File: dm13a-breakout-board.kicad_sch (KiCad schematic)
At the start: 6 parts, among them J1 Conn_01x16, J2 Conn_01x02, J3 Conn_01x05

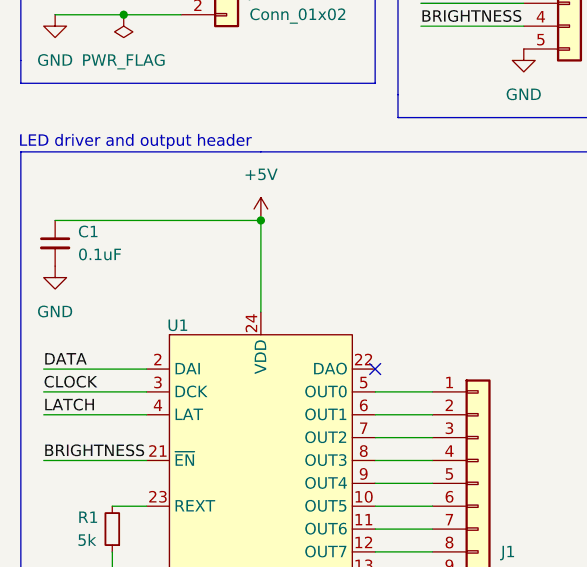
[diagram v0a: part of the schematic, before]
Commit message: Configure BOM stuff
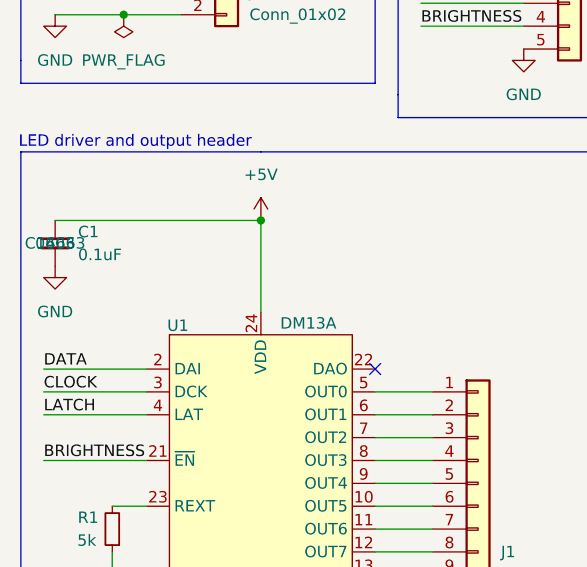
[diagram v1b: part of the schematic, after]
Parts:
- C1: JLCPCB package 0603 -> (none); JLCPCB part number C14663 -> (none); LCSC Part # (none) -> C14663; LCSC package (none) -> 0603
- U1: value ~ -> DM13A
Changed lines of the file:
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@@
-			)
-		)
-		(property "JLCPCB part number" ""
-			(at 24.13 83.82 0)
-			(effects
-				(font
-					(size 1.27 1.27)
-				)
 			)
 		)
@@
 			)
 		)
-		(property "JLCPCB part number" "C14663"
+		(property "LCSC package" "0603"
 			(at 17.78 52.07 0)
 			(effects
@@
 					(size 1.27 1.27)
 				)
-				(hide yes)
-			)
-		)
-		(property "JLCPCB package" "0603"
+			)
+		)
+		(property "LCSC Part #" "C14663"
 			(at 17.78 52.07 0)
 			(effects
@@
 					(size 1.27 1.27)
 				)
-				(hide yes)
 			)
 		)
@@
 			)
 		)
-		(property "JLCPCB part number" ""
-			(at 74.93 25.4 0)
-			(effects
-				(font
-					(size 1.27 1.27)
-				)
-			)
-		)
 		(pin "1"
 		)
@@
 			)
 		)
-		(property "JLCPCB part number" ""
-			(at 36.83 24.13 0)
-			(effects
-				(font
-					(size 1.27 1.27)
-				)
-			)
-		)
 		(pin "1"
 		)
@@
 			)
 		)
-		(property "JLCPCB part number" ""
-			(at 64.77 86.36 0)
-			(effects
-				(font
-					(size 1.27 1.27)
-				)
-			)
-		)
 		(pin "15"
 		)
@@
 			)
 		)
-		(property "Value" "~"
+		(property "Value" "DM13A"
 			(at 42.7833 60.96 0)
 			(effects
@@
 			)
 		)
-		(property "JLCPCB part number" ""
-			(at 40.64 86.36 0)
-			(effects
-				(font
-					(size 1.27 1.27)
-				)
-			)
-		)

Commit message: Try the whole thing
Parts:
- removed J1: Conn_01x16, symbol Connector_Generic:Conn_01x16
- added H1, H2, H3, H4: MountingHole, MountingHole:MountingHole_3.2mm_M3, symbol Mechanical:MountingHole
- added J3, J4: Conn_01x08, Connector_PinHeader_2.54mm:PinHeader_1x08_P2.54mm_Vertical, symbol Connector_Generic:Conn_01x08
- J1: renamed from J2; footprint (none) -> Connector_PinHeader_2.54mm:PinHeader_1x02_P2.54mm_Vertical
- J2: renamed from J3; footprint (none) -> Connector_PinHeader_2.54mm:PinHeader_1x05_P2.54mm_Vertical
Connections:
- net at U1.5 (OUT0): now also J3.1 (Pin_1)
- net at U1.14 (OUT9): now also J4.7 (Pin_7)
- net at U1.15 (OUT10): now also J4.6 (Pin_6)
- net at U1.16 (OUT11): now also J4.5 (Pin_5)
- net at U1.17 (OUT12): now also J4.4 (Pin_4)
- net at U1.18 (OUT13): now also J4.3 (Pin_3)
- net at U1.19 (OUT14): now also J4.2 (Pin_2)
- net at U1.20 (OUT15): now also J4.1 (Pin_1)
- net at U1.6 (OUT1): now also J3.2 (Pin_2)
- net at U1.7 (OUT2): now also J3.3 (Pin_3)
- net at U1.8 (OUT3): now also J3.4 (Pin_4)
- net at U1.9 (OUT4): now also J3.5 (Pin_5)
- net at U1.10 (OUT5): now also J3.6 (Pin_6)
- net at U1.11 (OUT6): now also J3.7 (Pin_7)
- net at U1.12 (OUT7): now also J3.8 (Pin_8)
- net at U1.13 (OUT8): now also J4.8 (Pin_8)
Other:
- note added: "Mounting holes"

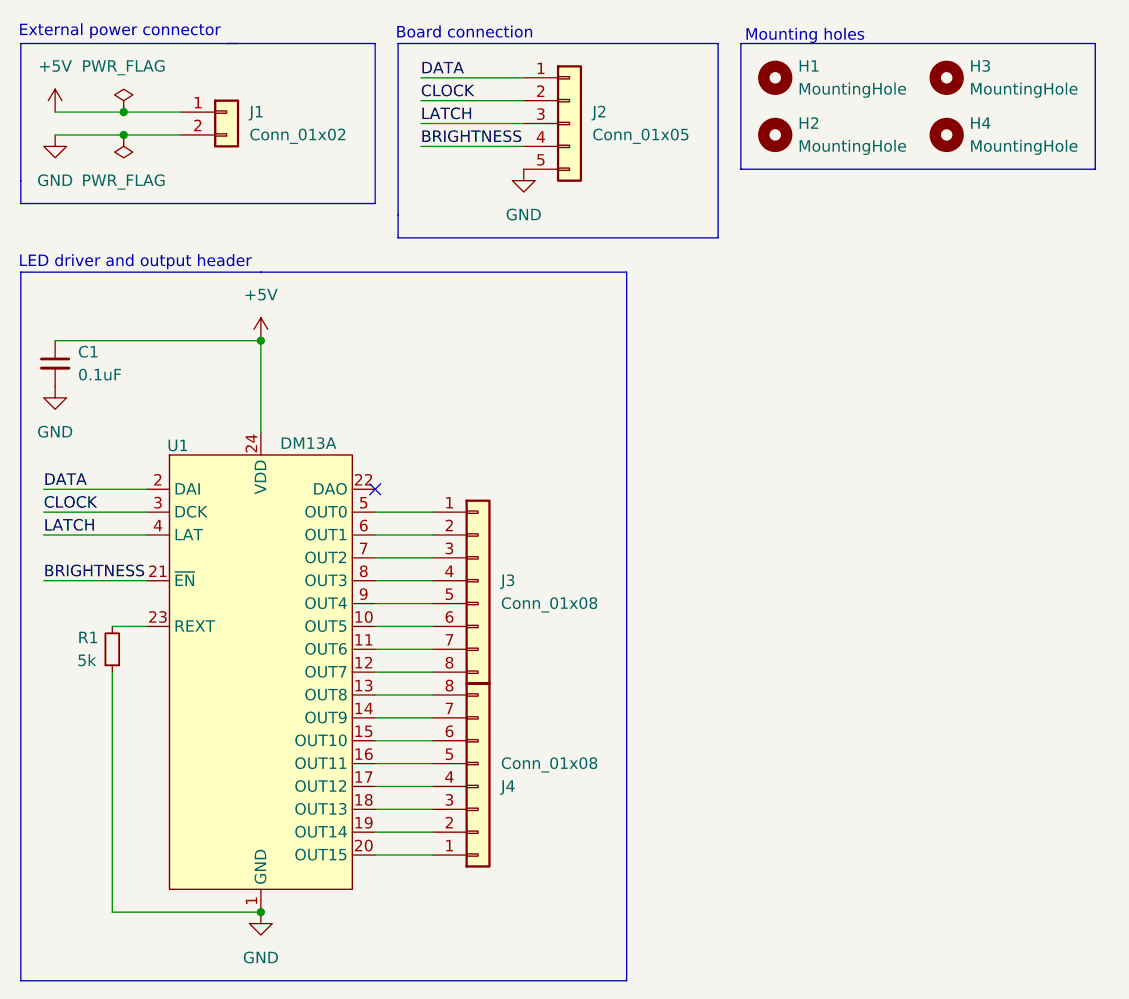
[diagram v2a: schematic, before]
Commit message: Use different connector, add gnd pins, add silkscreen
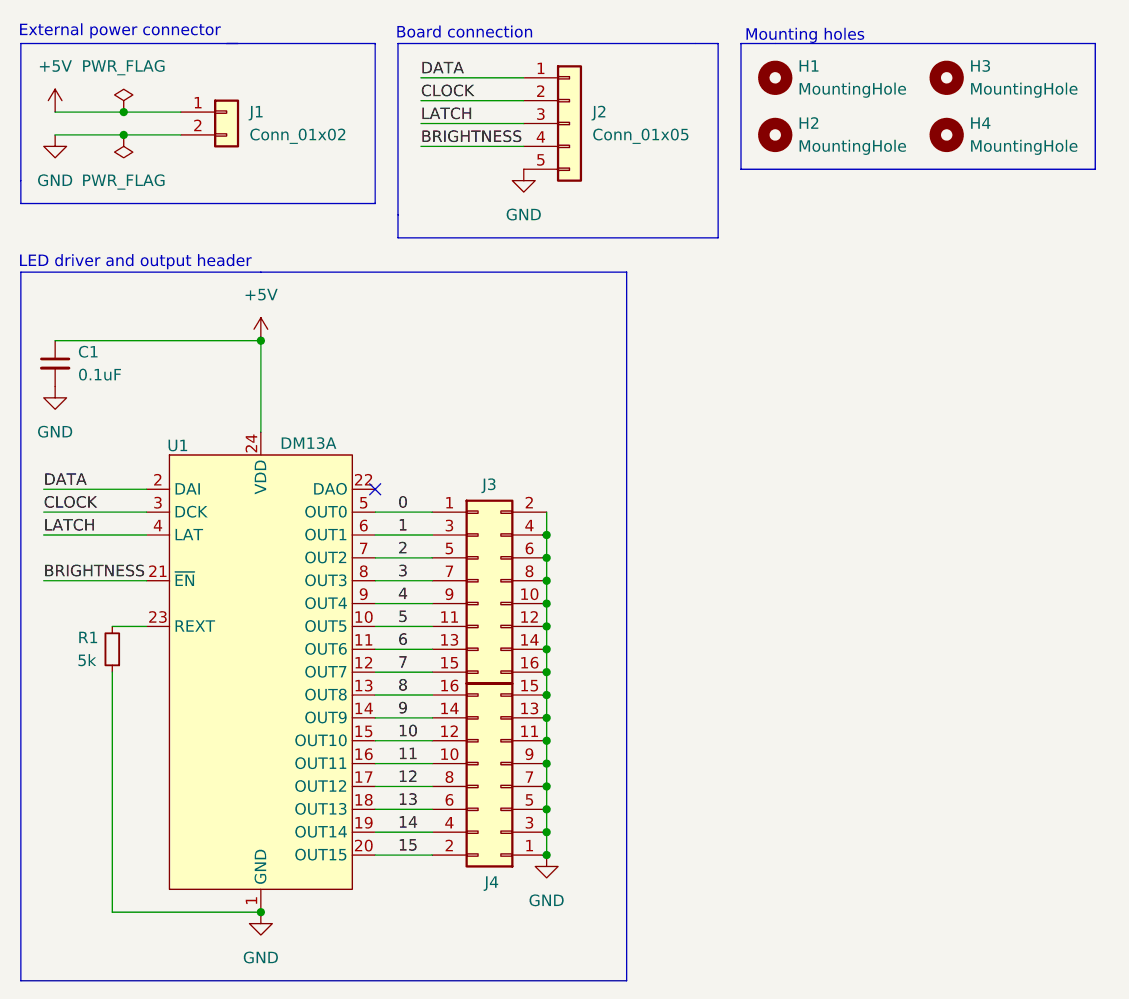
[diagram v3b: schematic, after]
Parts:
- removed J3, J4: Conn_01x08, Connector_PinHeader_2.54mm:PinHeader_1x08_P2.54mm_Vertical, symbol Connector_Generic:Conn_01x08
- added J3, J4: Conn_02x08_Odd_Even, Connector_PinSocket_2.54mm:PinSocket_2x08_P2.54mm_Vertical, symbol Connector_Generic:Conn_02x08_Odd_Even
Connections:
- net GND: now also J3.10 (Pin_10), J3.12 (Pin_12), J3.14 (Pin_14), J3.16 (Pin_16), J3.2 (Pin_2), J3.4 (Pin_4), J3.6 (Pin_6), J3.8 (Pin_8), J4.1 (Pin_1), J4.11 (Pin_11), J4.13 (Pin_13), J4.15 (Pin_15), J4.3 (Pin_3), J4.5 (Pin_5), J4.7 (Pin_7), J4.9 (Pin_9)
- net 15: now reaches U1.20 (OUT15)
- net 15: now also J4.2 (Pin_2)
- net 14: now reaches U1.19 (OUT14)
- net 14: now also J4.4 (Pin_4)
- net 13: now reaches U1.18 (OUT13)
- net 13: now also J4.6 (Pin_6)
- net 12: now reaches U1.17 (OUT12)
- net 12: now also J4.8 (Pin_8)
- net 11: now reaches U1.16 (OUT11)
- net 11: now also J4.10 (Pin_10)
- net 10: now reaches U1.15 (OUT10)
- net 10: now also J4.12 (Pin_12)
- net 9: now reaches U1.14 (OUT9)
- net 9: now also J4.14 (Pin_14)
- net 8: now reaches U1.13 (OUT8)
- net 8: now also J4.16 (Pin_16)
- net 0: now reaches U1.5 (OUT0)
- net 0: now also J3.1 (Pin_1)
- net 1: now reaches U1.6 (OUT1)
- net 1: now also J3.3 (Pin_3)
- net 2: now reaches U1.7 (OUT2)
- net 2: now also J3.5 (Pin_5)
- net 3: now reaches U1.8 (OUT3)
- net 3: now also J3.7 (Pin_7)
- net 4: now reaches U1.9 (OUT4)
- net 4: now also J3.9 (Pin_9)
- net 5: now reaches U1.10 (OUT5)
- net 5: now also J3.11 (Pin_11)
- net 6: now reaches U1.11 (OUT6)
- net 6: now also J3.13 (Pin_13)
- net 7: now reaches U1.12 (OUT7)
- net 7: now also J3.15 (Pin_15)
